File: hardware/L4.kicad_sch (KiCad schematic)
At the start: 61 parts, among them J1 Conn_01x02, Q1 Q_PMOS_GSD, SW1 SW_Push, SW10 SW_Push, SW11 SW_Push, SW12 SW_Push, SW13 SW_Push, SW14 SW_Push, SW15 SW_Push, SW16 SW_Push, SW17 SW_Push, SW18 SW_Push, SW19 SW_Push, SW2 SW_Push, SW20 SW_Push, SW21 SW_Push, SW22 SW_Push, SW23 SW_Push, SW24 SW_Push, SW25 SW_Push, SW26 SW_Push, SW27 SW_DP3T, SW3 SW_Push, SW4 SW_Push, SW5 SW_Push, SW6 SW_Push, SW7 SW_Push, SW8 SW_Push, SW9 SW_Push, U1 XIAO nRF52840

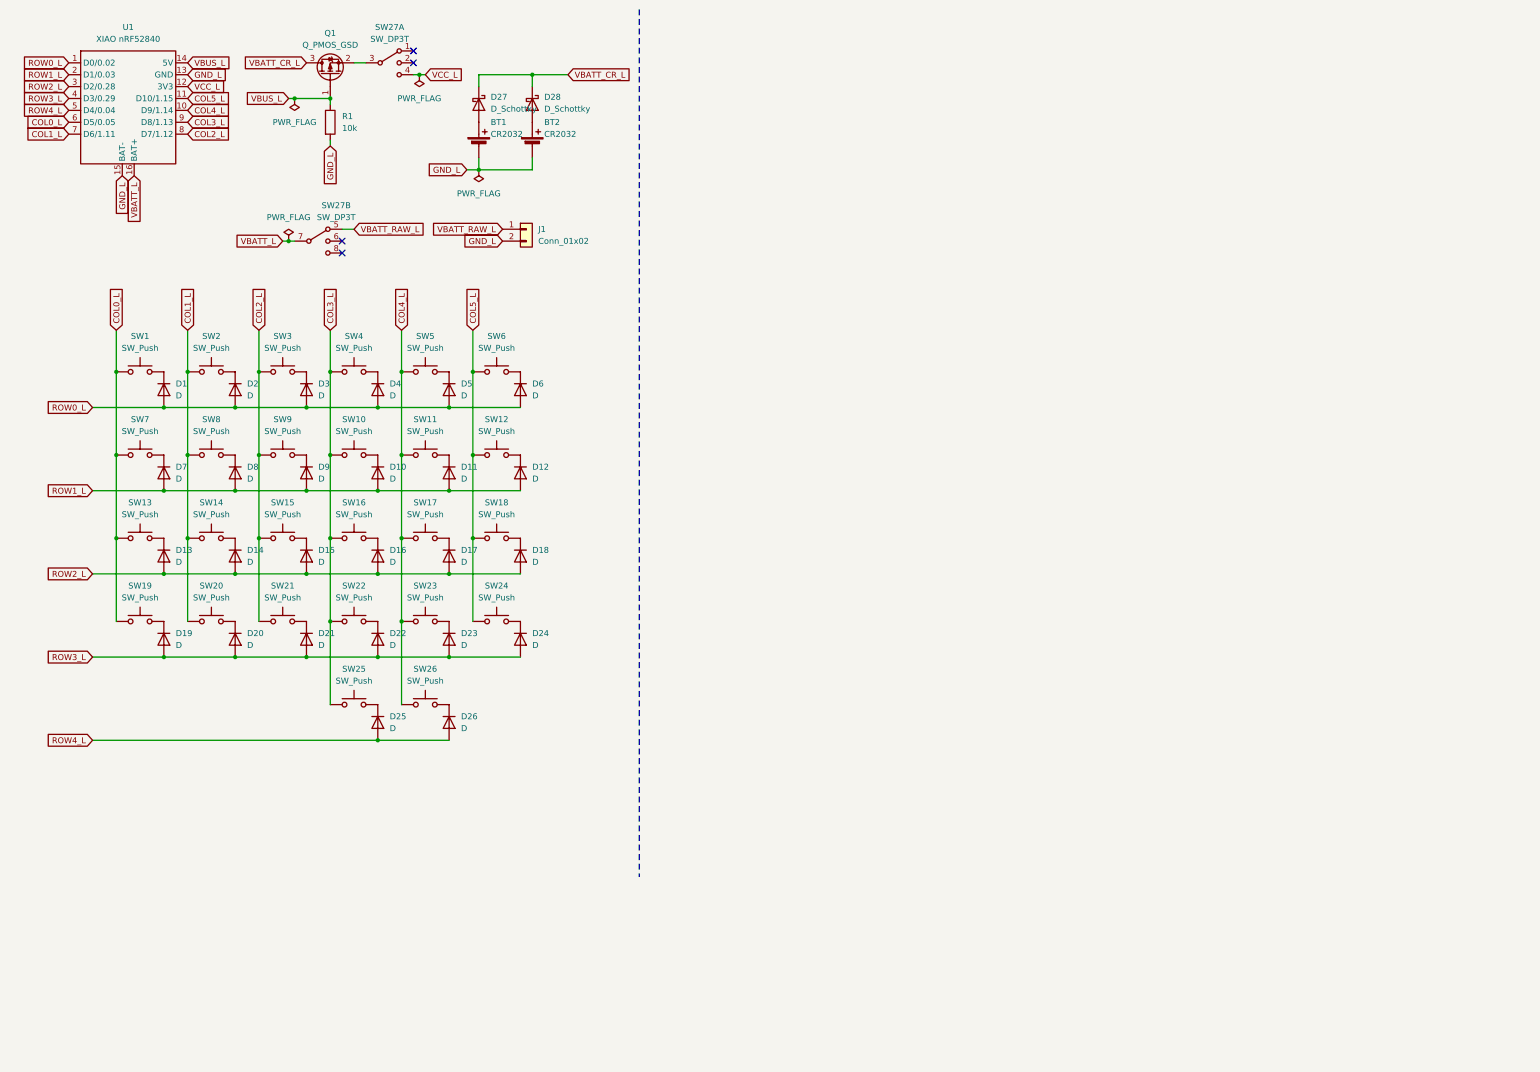
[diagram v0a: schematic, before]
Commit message: finish right halve
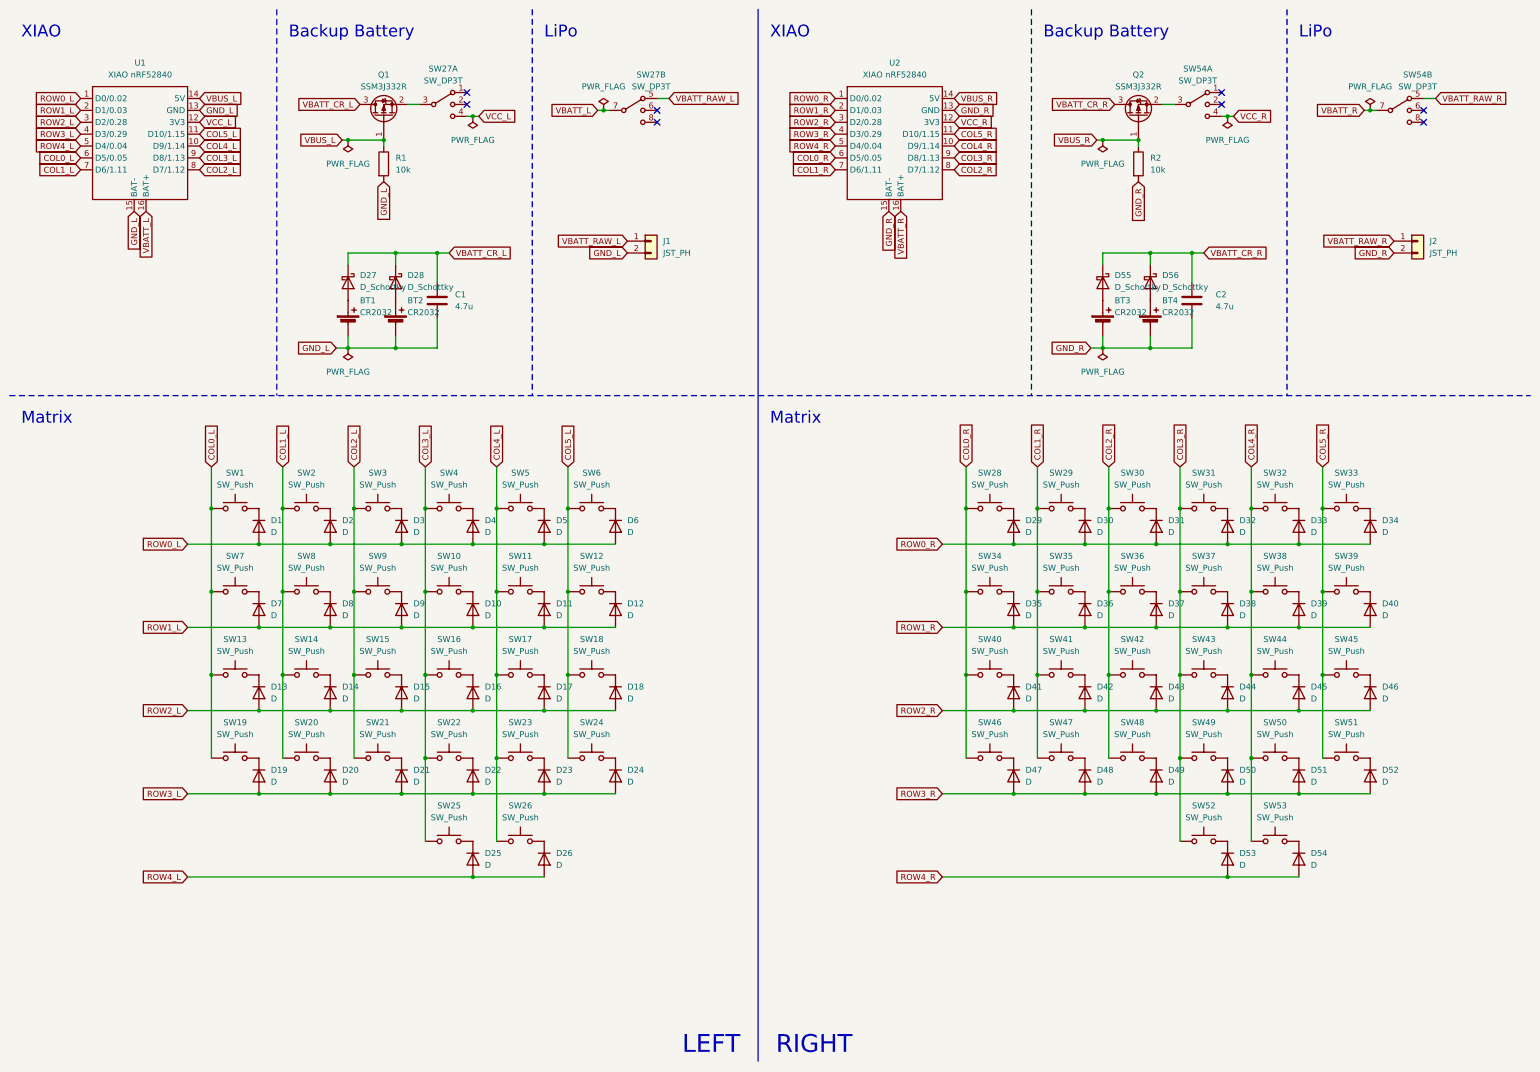
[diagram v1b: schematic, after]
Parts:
- added BT3, BT4: CR2032, symbol Device:Battery_Cell
- added C1, C2: 4.7u, symbol Device:C
- added D29, D30, D31, D32, D33, D34, D35, D36, D37, D38, D39, D40, D41, D42, D43, D44, D45, D46, D47, D48, D49, D50, D51, D52, D53, D54: D, symbol Device:D
- added D55, D56: D_Schottky, symbol Device:D_Schottky
- added J2: JST_PH, symbol Connector_Generic:Conn_01x02
- added Q2: SSM3J332R, symbol Device:Q_PMOS_GSD
- added R2: 10k, symbol Device:R
- added SW28, SW29, SW30, SW31, SW32, SW33, SW34, SW35, SW36, SW37, SW38, SW39, SW40, SW41, SW42, SW43, SW44, SW45, SW46, SW47, SW48, SW49, SW50, SW51, SW52, SW53: SW_Push, symbol Switch:SW_Push
- added SW54: SW_DP3T, symbol Switch:SW_DP3T
- added U2: XIAO nRF52840, symbol seeed:xiao_nrf52840
- J1: value Conn_01x02 -> JST_PH
- Q1: value Q_PMOS_GSD -> SSM3J332R
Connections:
- net GND_L: now also C1.2
- net VBATT_CR_L: now also C1.1
- new net: D49.1 (K), SW48.2
- new net: D44.1 (K), SW43.2
- new net: D37.1 (K), SW36.2
- new net: BT4.1 (+), D56.2 (A)
- new net: BT3.1 (+), D55.2 (A)
- new net: D54.1 (K), SW53.2
- new net: D39.1 (K), SW38.2
- new net: D34.1 (K), SW33.2
- new net: D43.1 (K), SW42.2
- new net: D45.1 (K), SW44.2
- new net: D47.1 (K), SW46.2
- new net: D40.1 (K), SW39.2
- new net: D33.1 (K), SW32.2
- new net: D52.1 (K), SW51.2
- new net: D32.1 (K), SW31.2
- new net: Q2.2 (S), SW54.3
- new net: D31.1 (K), SW30.2
- new net: D42.1 (K), SW41.2
- new net: D48.1 (K), SW47.2
- new net: D41.1 (K), SW40.2
- new net: D53.1 (K), SW52.2
- new net: D36.1 (K), SW35.2
- new net: D51.1 (K), SW50.2
- new net: D38.1 (K), SW37.2
- new net: D50.1 (K), SW49.2
- new net: D46.1 (K), SW45.2
- new net: D30.1 (K), SW29.2
- new net: D29.1 (K), SW28.2
- new net: D35.1 (K), SW34.2
- new net COL0_R: SW28.1, SW34.1, SW40.1, SW46.1, U2.6 (D5/0.05)
- new net COL1_R: SW29.1, SW35.1, SW41.1, SW47.1, U2.7 (D6/1.11)
- new net COL2_R: SW30.1, SW36.1, SW42.1, SW48.1, U2.8 (D7/1.12)
- new net COL3_R: SW31.1, SW37.1, SW43.1, SW49.1, SW52.1, U2.9 (D8/1.13)
- new net COL4_R: SW32.1, SW38.1, SW44.1, SW50.1, SW53.1, U2.10 (D9/1.14)
- new net COL5_R: SW33.1, SW39.1, SW45.1, SW51.1, U2.11 (D10/1.15)
- new net GND_R: BT3.2 (-), BT4.2 (-), C2.2, J2.2 (Pin_2), R2.2, U2.13 (GND), U2.15 (BAT-)
- new net ROW0_R: D29.2 (A), D30.2 (A), D31.2 (A), D32.2 (A), D33.2 (A), D34.2 (A), U2.1 (D0/0.02)
- new net ROW1_R: D35.2 (A), D36.2 (A), D37.2 (A), D38.2 (A), D39.2 (A), D40.2 (A), U2.2 (D1/0.03)
- new net ROW2_R: D41.2 (A), D42.2 (A), D43.2 (A), D44.2 (A), D45.2 (A), D46.2 (A), U2.3 (D2/0.28)
- new net ROW3_R: D47.2 (A), D48.2 (A), D49.2 (A), D50.2 (A), D51.2 (A), D52.2 (A), U2.4 (D3/0.29)
- new net ROW4_R: D53.2 (A), D54.2 (A), U2.5 (D4/0.04)
- new net VBATT_CR_R: C2.1, D55.1 (K), D56.1 (K), Q2.3 (D)
- new net VBATT_R: SW54.7, U2.16 (BAT+)
- new net VBATT_RAW_R: J2.1 (Pin_1), SW54.5
- new net VBUS_R: Q2.1 (G), R2.1, U2.14 (5V)
- new net VCC_R: SW54.4, U2.12 (3V3)
- no-connect marks 4 -> 8
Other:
- note added: "Backup Battery"
- note added: "LEFT"
- note added: "LiPo"
- note added: "Matrix"
- note added: "RIGHT"
- note added: "XIAO"
- moved on the sheet: BT1, BT2, D1, D10, D11, D12, D13, D14, D15, D16, D17, D18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

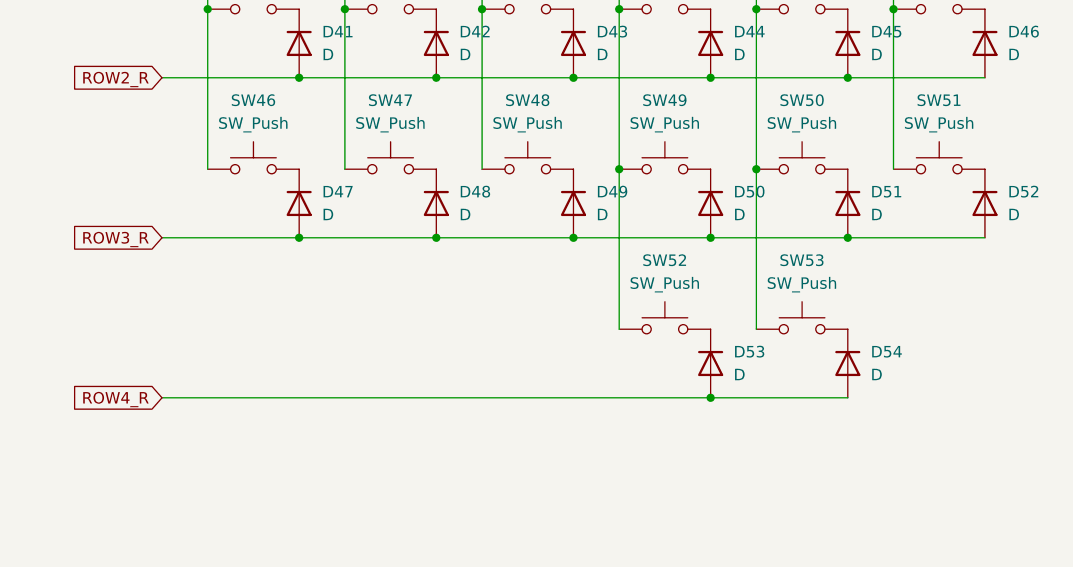
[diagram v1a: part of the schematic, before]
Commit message: fix switch position
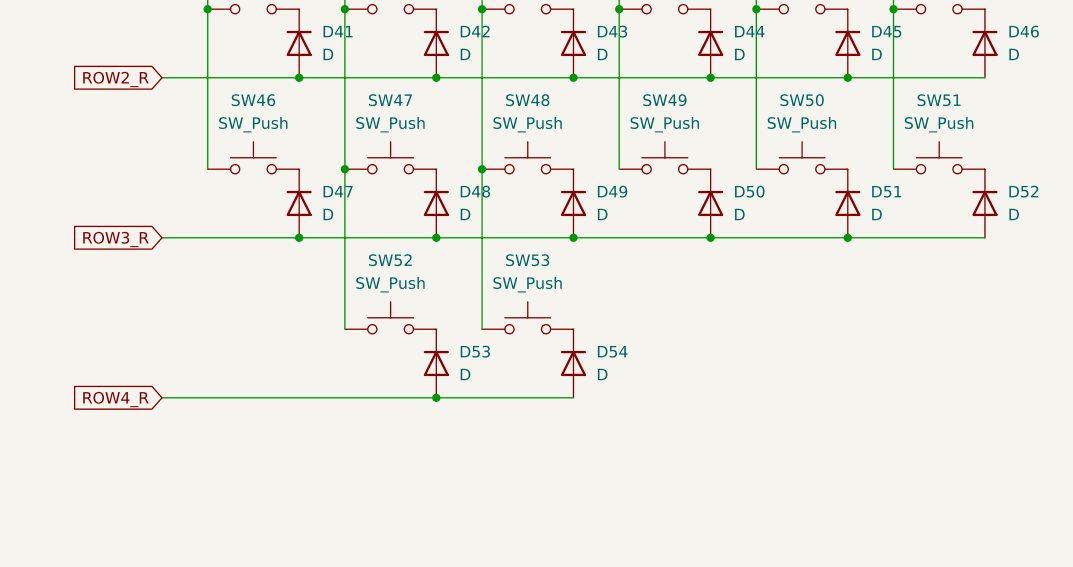
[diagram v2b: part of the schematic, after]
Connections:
- net COL1_R: now also SW52.1
- net COL2_R: now also SW53.1
- net COL3_R: no longer SW52.1
- net COL4_R: no longer SW53.1
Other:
- moved on the sheet: D53, D54, SW52, SW53
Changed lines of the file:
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@@
   (junction (at 101.6 119.38) (diameter 0) (color 0 0 0 0)
   )
-  (junction (at 278.13 172.72) (diameter 0) (color 0 0 0 0)
-  )
   (junction (at 262.89 137.16) (diameter 0) (color 0 0 0 0)
   )
@@
   (junction (at 288.29 162.56) (diameter 0) (color 0 0 0 0)
   )
+  (junction (at 232.41 172.72) (diameter 0) (color 0 0 0 0)
+  )
   (junction (at 132.08 119.38) (diameter 0) (color 0 0 0 0)
   )
@@
   (junction (at 111.76 198.12) (diameter 0) (color 0 0 0 0)
   )
-  (junction (at 273.05 198.12) (diameter 0) (color 0 0 0 0)
-  )
   (junction (at 247.65 119.38) (diameter 0) (color 0 0 0 0)
   )
@@
   (junction (at 257.81 144.78) (diameter 0) (color 0 0 0 0)
   )
+  (junction (at 247.65 172.72) (diameter 0) (color 0 0 0 0)
+  )
   (junction (at 246.38 85.09) (diameter 0) (color 0 0 0 0)
   )
   (junction (at 96.52 180.34) (diameter 0) (color 0 0 0 0)
   )
+  (junction (at 242.57 198.12) (diameter 0) (color 0 0 0 0)
+  )
   (junction (at 293.37 137.16) (diameter 0) (color 0 0 0 0)
   )
@@
   )
   (junction (at 127 162.56) (diameter 0) (color 0 0 0 0)
-  )
-  (junction (at 262.89 172.72) (diameter 0) (color 0 0 0 0)
   )
   (junction (at 96.52 162.56) (diameter 0) (color 0 0 0 0)
@@
     (stroke (width 0) (type default))
   )
-  (wire (pts (xy 278.13 172.72) (xy 278.13 190.5))
-    (stroke (width 0) (type default))
-  )
   (wire (pts (xy 227.33 127) (xy 242.57 127))
     (stroke (width 0) (type default))
@@
     (stroke (width 0) (type solid))
   )
-  (wire (pts (xy 262.89 172.72) (xy 262.89 190.5))
-    (stroke (width 0) (type default))
-  )
   (wire (pts (xy 139.7 34.29) (xy 140.97 34.29))
     (stroke (width 0) (type default))
@@
     (stroke (width 0) (type default))
   )
+  (wire (pts (xy 242.57 198.12) (xy 257.81 198.12))
+    (stroke (width 0) (type default))
+  )
   (wire (pts (xy 71.12 154.94) (xy 71.12 172.72))
     (stroke (width 0) (type default))
@@
     (stroke (width 0) (type default))
   )
-  (wire (pts (xy 273.05 198.12) (xy 288.29 198.12))
-    (stroke (width 0) (type default))
-  )
   (wire (pts (xy 50.8 162.56) (xy 66.04 162.56))
     (stroke (width 0) (type default))
@@
     (stroke (width 0) (type default))
   )
+  (wire (pts (xy 232.41 172.72) (xy 232.41 190.5))
+    (stroke (width 0) (type default))
+  )
   (wire (pts (xy 85.09 40.64) (xy 92.71 40.64))
     (stroke (width 0) (type default))
@@
     (stroke (width 0) (type default))
   )
+  (wire (pts (xy 247.65 172.72) (xy 247.65 190.5))
+    (stroke (width 0) (type default))
+  )
   (wire (pts (xy 278.13 137.16) (xy 278.13 154.94))
     (stroke (width 0) (type default))
@@
     (stroke (width 0) (type default))
   )
-  (wire (pts (xy 212.09 198.12) (xy 273.05 198.12))
+  (wire (pts (xy 212.09 198.12) (xy 242.57 198.12))
     (stroke (width 0) (type default))
   )
@@
     )
   )
-  (symbol (lib_id "Switch:SW_Push") (at 283.21 190.5 0) (unit 1)
-    (in_bom yes) (on_board yes) (dnp no) (fields_autoplaced)
-    (property "Reference" "SW53" (at 283.21 182.88 0)
-      (effects (font (size 1.27 1.27)))
-    )
-    (property "Value" "SW_Push" (at 283.21 185.42 0)
-      (effects (font (size 1.27 1.27)))
-    )
-    (property "Footprint" "" (at 283.21 185.42 0)
-      (effects (font (size 1.27 1.27)) hide)
-    )
-    (property "Datasheet" "~" (at 283.21 185.42 0)
+  (symbol (lib_id "Switch:SW_Push") (at 252.73 190.5 0) (unit 1)
+    (in_bom yes) (on_board yes) (dnp no) (fields_autoplaced)
+    (property "Reference" "SW53" (at 252.73 182.88 0)
+      (effects (font (size 1.27 1.27)))
+    )
+    (property "Value" "SW_Push" (at 252.73 185.42 0)
+      (effects (font (size 1.27 1.27)))
+    )
+    (property "Footprint" "" (at 252.73 185.42 0)
+      (effects (font (size 1.27 1.27)) hide)
+    )
+    (property "Datasheet" "~" (at 252.73 185.42 0)
       (effects (font (size 1.27 1.27)) hide)
     )
@@
     )
   )
-  (symbol (lib_id "Device:D") (at 288.29 194.31 270) (unit 1)
-    (in_bom yes) (on_board yes) (dnp no) (fields_autoplaced)
-    (property "Reference" "D54" (at 290.83 193.04 90)
-      (effects (font (size 1.27 1.27)) (justify left))
-    )
-    (property "Value" "D" (at 290.83 195.58 90)
-      (effects (font (size 1.27 1.27)) (justify left))
-    )
-    (property "Footprint" "" (at 288.29 194.31 0)
-      (effects (font (size 1.27 1.27)) hide)
-    )
-    (property "Datasheet" "~" (at 288.29 194.31 0)
-      (effects (font (size 1.27 1.27)) hide)
-    )
-    (property "Sim.Device" "D" (at 288.29 194.31 0)
-      (effects (font (size 1.27 1.27)) hide)
-    )
-    (property "Sim.Pins" "1=K 2=A" (at 288.29 194.31 0)
+  (symbol (lib_id "Device:D") (at 257.81 194.31 270) (unit 1)
+    (in_bom yes) (on_board yes) (dnp no) (fields_autoplaced)
+    (property "Reference" "D54" (at 260.35 193.04 90)
+      (effects (font (size 1.27 1.27)) (justify left))
+    )
+    (property "Value" "D" (at 260.35 195.58 90)
+      (effects (font (size 1.27 1.27)) (justify left))
+    )
+    (property "Footprint" "" (at 257.81 194.31 0)
+      (effects (font (size 1.27 1.27)) hide)
+    )
+    (property "Datasheet" "~" (at 257.81 194.31 0)
+      (effects (font (size 1.27 1.27)) hide)
+    )
+    (property "Sim.Device" "D" (at 257.81 194.31 0)
+      (effects (font (size 1.27 1.27)) hide)
+    )
+    (property "Sim.Pins" "1=K 2=A" (at 257.81 194.31 0)
       (effects (font (size 1.27 1.27)) hide)
     )
@@
     )
   )
-  (symbol (lib_id "Switch:SW_Push") (at 267.97 190.5 0) (unit 1)
-    (in_bom yes) (on_board yes) (dnp no) (fields_autoplaced)
-    (property "Reference" "SW52" (at 267.97 182.88 0)
-      (effects (font (size 1.27 1.27)))
-    )
-    (property "Value" "SW_Push" (at 267.97 185.42 0)
-      (effects (font (size 1.27 1.27)))
-    )
-    (property "Footprint" "" (at 267.97 185.42 0)
-      (effects (font (size 1.27 1.27)) hide)
-    )
-    (property "Datasheet" "~" (at 267.97 185.42 0)
+  (symbol (lib_id "Switch:SW_Push") (at 237.49 190.5 0) (unit 1)
+    (in_bom yes) (on_board yes) (dnp no) (fields_autoplaced)
+    (property "Reference" "SW52" (at 237.49 182.88 0)
+      (effects (font (size 1.27 1.27)))
+    )
+    (property "Value" "SW_Push" (at 237.49 185.42 0)
+      (effects (font (size 1.27 1.27)))
+    )
+    (property "Footprint" "" (at 237.49 185.42 0)
+      (effects (font (size 1.27 1.27)) hide)
+    )
+    (property "Datasheet" "~" (at 237.49 185.42 0)
       (effects (font (size 1.27 1.27)) hide)
     )
@@
     )
   )
-  (symbol (lib_id "Device:D") (at 273.05 194.31 270) (unit 1)
-    (in_bom yes) (on_board yes) (dnp no) (fields_autoplaced)
-    (property "Reference" "D53" (at 275.59 193.04 90)
-      (effects (font (size 1.27 1.27)) (justify left))
-    )
-    (property "Value" "D" (at 275.59 195.58 90)
-      (effects (font (size 1.27 1.27)) (justify left))
-    )
-    (property "Footprint" "" (at 273.05 194.31 0)
-      (effects (font (size 1.27 1.27)) hide)
-    )
-    (property "Datasheet" "~" (at 273.05 194.31 0)
-      (effects (font (size 1.27 1.27)) hide)
-    )
-    (property "Sim.Device" "D" (at 273.05 194.31 0)
-      (effects (font (size 1.27 1.27)) hide)
-    )
-    (property "Sim.Pins" "1=K 2=A" (at 273.05 194.31 0)
-      (effects (font (size 1.27 1.27)) hide)
-    )
+  (symbol (lib_id "Device:D") (at 242.57 194.31 270) (unit 1)
+    (in_bom yes) (on_board yes) (dnp no) (fields_autoplaced)
+    (property "Reference" "D53" (at 245.11 193.04 90)
+      (effects (font (size 1.27 1.27)) (justify left))
+    )
+    (property "Value" "D" (at 245.11 195.58 90)
+      (effects (font (size 1.27 1.27)) (justify left))
+    )
+    (property "Footprint" "" (at 242.57 194.31 0)
+      (effects (font (size 1.27 1.27)) hide)
+    )
+    (property "Datasheet" "~" (at 242.57 194.31 0)
+      (effects (font (size 1.27 1.27)) hide)
+    )
+    (property "Sim.Device" "D" (at 242.57 194.31 0)
+      (effects (font (size 1.27 1.27)) hide)
+    )
+    (property "Sim.Pins" "1=K 2=A" (at 242.57 194.31 0)
+      (effects (font (size 1.27 1.27)) hide)
+    )

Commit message: link footprints
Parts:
- BT1, BT2, BT3, BT4: footprint (none) -> Battery:BatteryHolder_Multicomp_BC-2001_1x2032
- C1, C2: footprint (none) -> Capacitor_SMD:C_0805_2012Metric_Pad1.18x1.45mm_HandSolder
- D1, D10, D11, D12, D13, D14, D15, D16, D17, D18, D19, D2, D20, D21, D22, D23, D24, D25, D26, D27, D28, D29, D3, D30, D31, D32, D33, D34, D35, D36, D37, D38, D39, D4, D40, D41, D42, D43, D44, D45, D46, D47, D48, D49, D5, D50, D51, D52, D53, D54, D55, D56, D6, D7, D8, D9: footprint (none) -> Diode_SMD:D_SOD-123
- J1, J2: footprint (none) -> Connector_JST:JST_PH_S2B-PH-K_1x02_P2.00mm_Horizontal
- Q1, Q2: footprint (none) -> Package_TO_SOT_SMD:SOT-23-3
- R1, R2: footprint (none) -> Resistor_THT:R_Axial_DIN0207_L6.3mm_D2.5mm_P7.62mm_Horizontal
- SW1, SW10, SW11, SW12, SW13, SW14, SW15, SW16, SW17, SW18, SW19, SW2, SW20, SW21, SW22, SW23, SW24, SW25, SW26, SW28, SW29, SW3, SW30, SW31, SW32, SW33, SW34, SW35, SW36, SW37, SW38, SW39, SW4, SW40, SW41, SW42, SW43, SW44, SW45, SW46, SW47, SW48, SW49, SW5, SW50, SW51, SW52, SW53, SW6, SW7, SW8, SW9: footprint (none) -> kbd:keyswitch_cherrymx_choc12_1u
- SW27, SW54: footprint (none) -> akizuki:MSS23D18
- U1, U2: footprint (none) -> akizuki:XIAO_nrf52840
